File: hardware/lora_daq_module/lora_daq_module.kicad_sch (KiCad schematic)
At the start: 0 parts

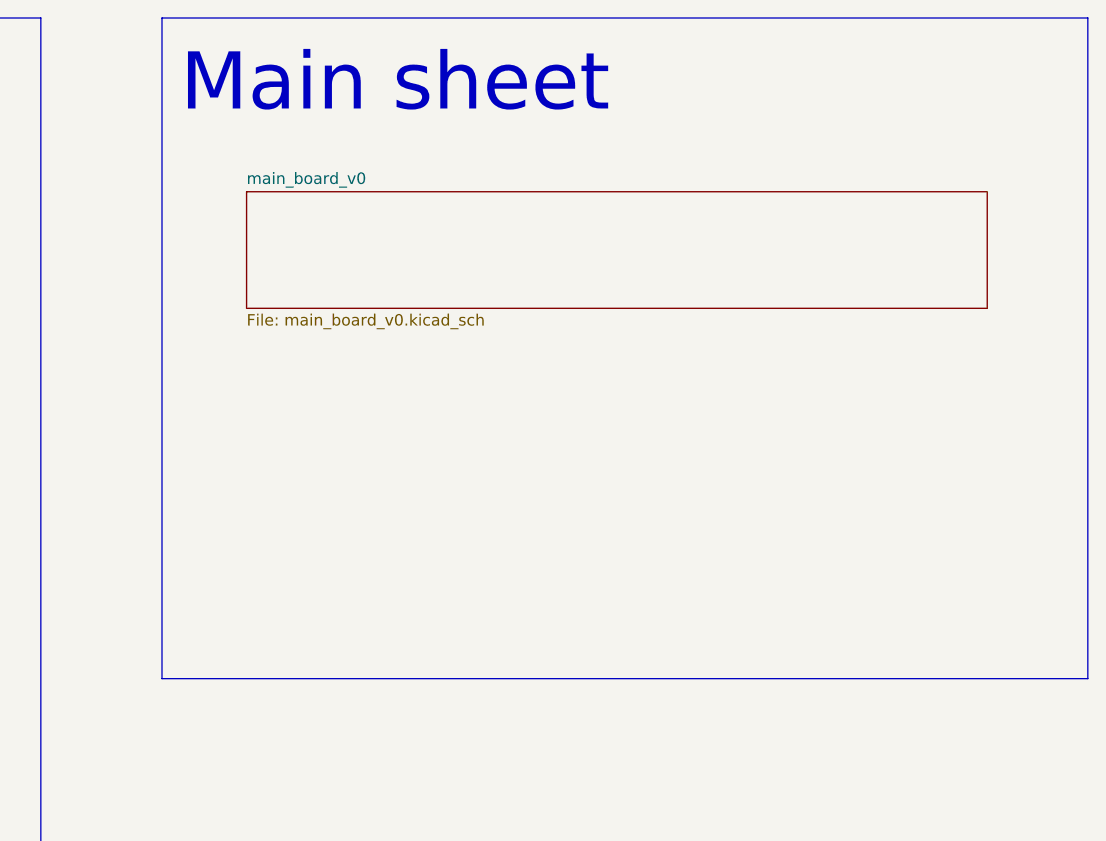
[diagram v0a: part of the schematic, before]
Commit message: updated power schematic to include power switching IC for battery/usb power, minor changes to lora module schematic, added footprints to all component and began with the preliminary layout based on data sheet and application note reccomendations for each component.
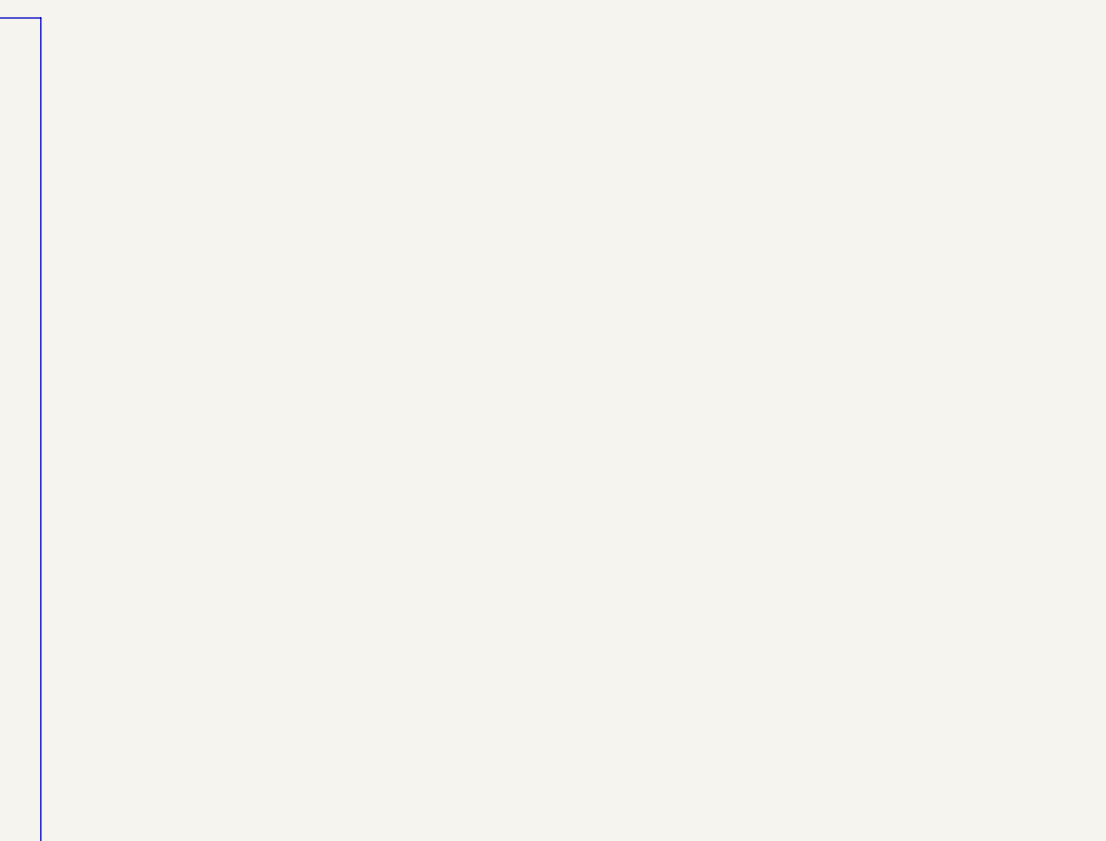
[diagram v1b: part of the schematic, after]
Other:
- removed sheet main_board_v0
- note removed: "Main sheet"
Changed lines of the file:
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@@
-		)
-	)
-	(rectangle
-		(start 175.514 26.924)
-		(end 278.384 100.33)
-		(stroke
-			(width 0)
-			(type default)
-		)
-		(fill
-			(type none)
-		)
-	)
-	(text "Main sheet"
-		(exclude_from_sim no)
-		(at 177.546 34.29 0)
-		(effects
-			(font
-				(size 6.35 6.35)
-				(color 0 0 255 1)
-			)
-			(justify left)
 		)
 	)
@@
 				)
 			)
-		)
-	)
-	(sheet
-		(at 184.912 46.228)
-		(size 82.296 12.954)
-		(exclude_from_sim no)
-		(in_bom yes)
-		(on_board yes)
-		(dnp no)
-		(fields_autoplaced yes)
-		(stroke
-			(width 0.1524)
-			(type solid)
-		)
-		(fill
-			(color 0 0 0 0.0000)
-		)
-		(property "Sheetname" "main_board_v0"
-			(at 184.912 45.5164 0)
-			(effects
-				(font
-					(size 1.27 1.27)
-				)
-				(justify left bottom)
-			)
-		)
-		(property "Sheetfile" "main_board_v0.kicad_sch"
-			(at 184.912 59.7666 0)
-			(effects
-				(font
-					(size 1.27 1.27)
-				)
-				(justify left top)
-			)
-		)
-		(instances
-			(project "lora_daq_module"
-				(path "/3a75d17e-6505-4097-95c7-feffd430343e"
-					(page "5")
-				)
-			)
